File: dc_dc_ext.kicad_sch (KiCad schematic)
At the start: 30 parts, among them U10 TPS56339DDC, U11 TPS56339DDC

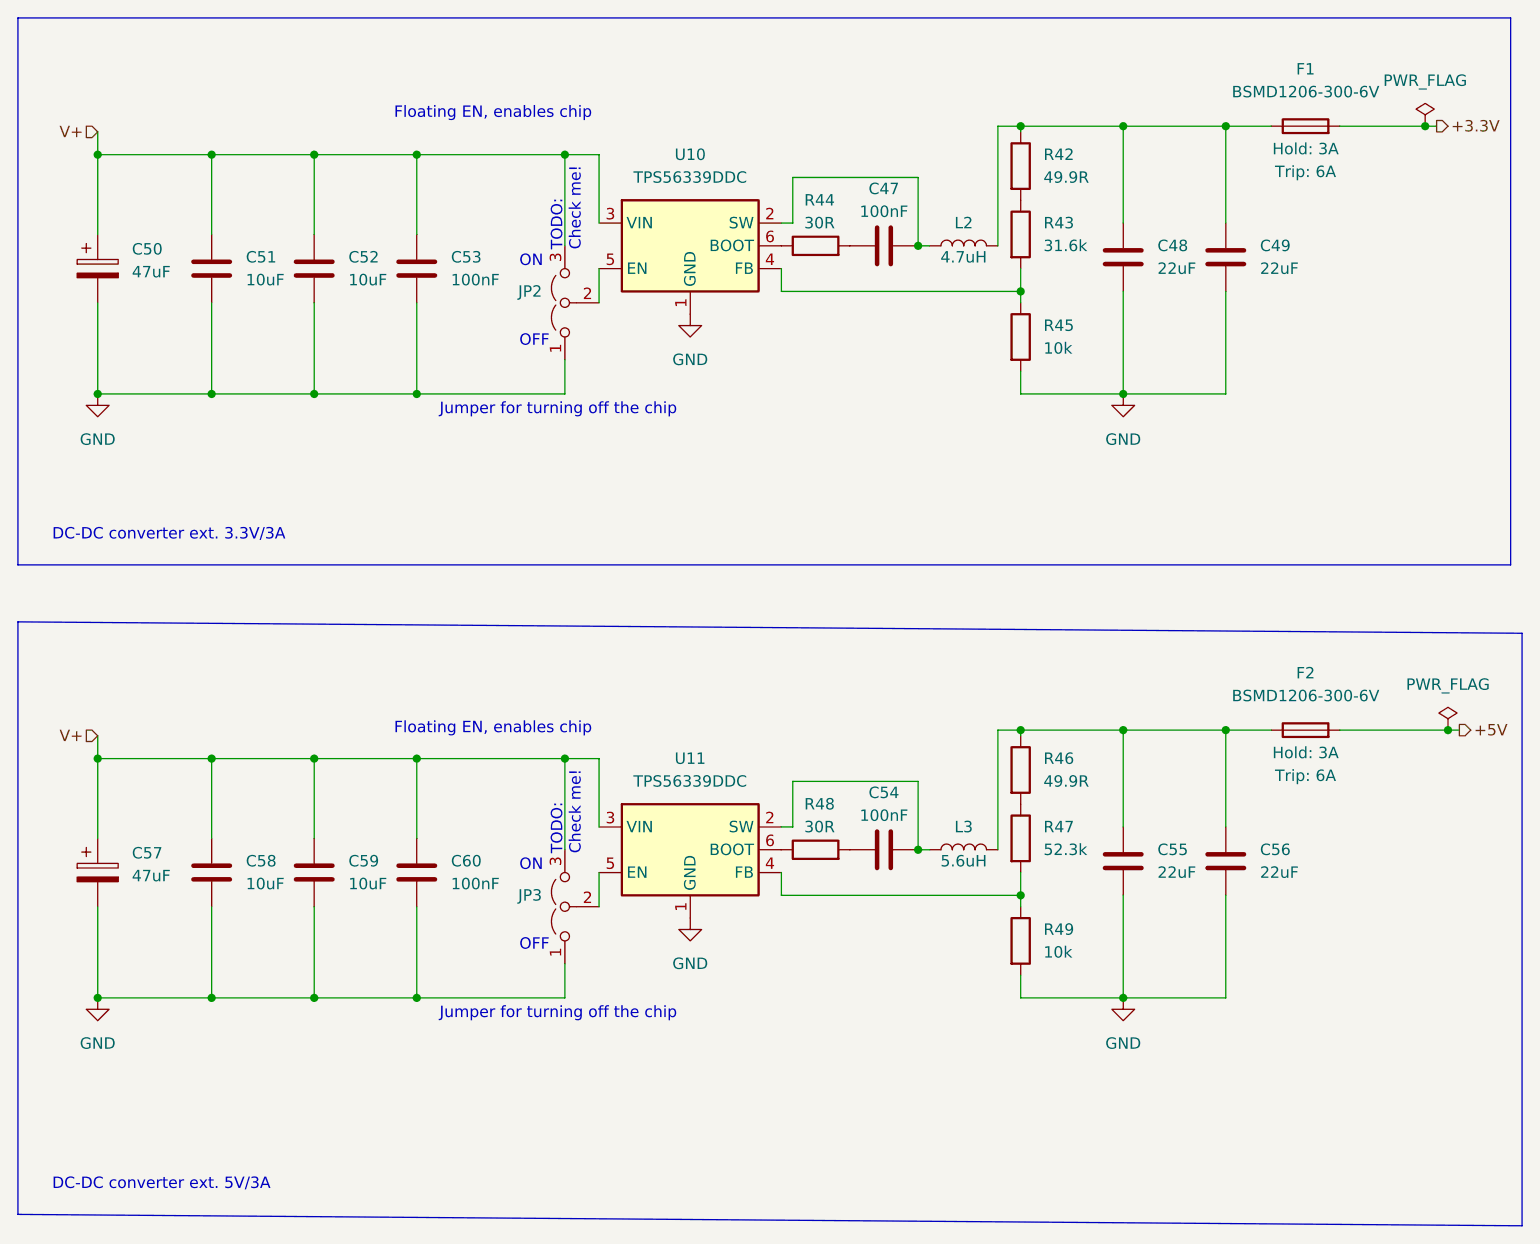
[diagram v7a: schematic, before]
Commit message: optimized component selection, assigned missing LCSC part numbers
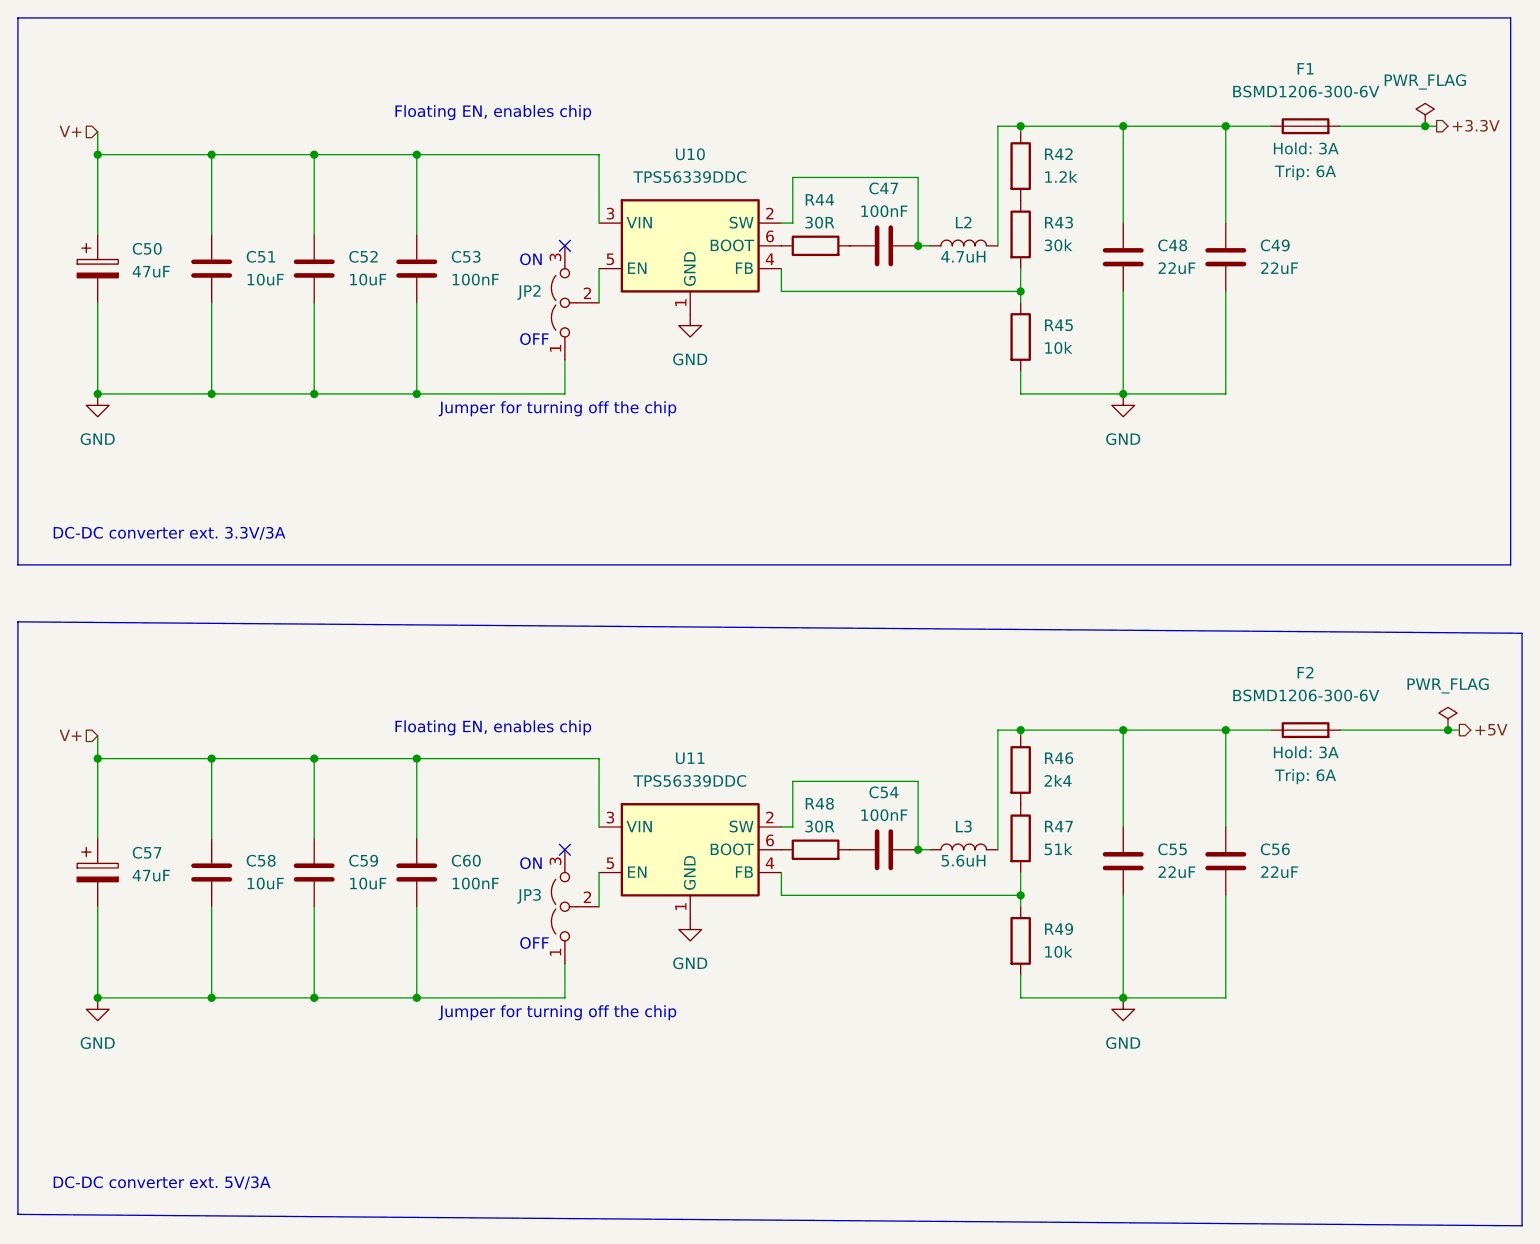
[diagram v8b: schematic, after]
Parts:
- C47, C53, C54, C60: footprint Capacitor_SMD:C_0805_2012Metric_Pad1.18x1.45mm_HandSolder -> Capacitor_SMD:C_0805_2012Metric
- C48, C49, C55, C56: footprint Capacitor_SMD:C_0805_2012Metric_Pad1.18x1.45mm_HandSolder -> Capacitor_SMD:C_1206_3216Metric; LCSC (none) -> C49217
- C50, C57: footprint Capacitor_SMD:CP_Elec_6.3x5.8 -> Capacitor_SMD:C_1206_3216Metric; LCSC (none) -> C403725
- C51, C52, C58, C59: footprint Capacitor_SMD:C_1206_3216Metric_Pad1.33x1.80mm_HandSolder -> Capacitor_SMD:C_1206_3216Metric; LCSC (none) -> C13585
- F1, F2: LCSC (none) -> C883136
- L2: LCSC (none) -> C167220
- L3: LCSC (none) -> C386869
- R42: value 49.9R -> 1.2k; footprint Resistor_SMD:R_0805_2012Metric_Pad1.20x1.40mm_HandSolder -> Resistor_SMD:R_0603_1608Metric; LCSC (none) -> C22765
- R43: value 31.6k -> 30k; footprint Resistor_SMD:R_0805_2012Metric_Pad1.20x1.40mm_HandSolder -> Resistor_SMD:R_0603_1608Metric; LCSC (none) -> C22984
- R44, R48: footprint Resistor_SMD:R_0805_2012Metric_Pad1.20x1.40mm_HandSolder -> Resistor_SMD:R_0603_1608Metric; LCSC (none) -> C23140
- R45, R49: footprint Resistor_SMD:R_0805_2012Metric_Pad1.20x1.40mm_HandSolder -> Resistor_SMD:R_0603_1608Metric; LCSC (none) -> C25804
- R46: value 49.9R -> 2k4; footprint Resistor_SMD:R_0805_2012Metric_Pad1.20x1.40mm_HandSolder -> Resistor_SMD:R_0603_1608Metric; LCSC (none) -> C22940
- R47: value 52.3k -> 51k; footprint Resistor_SMD:R_0805_2012Metric_Pad1.20x1.40mm_HandSolder -> Resistor_SMD:R_0603_1608Metric; LCSC (none) -> C23196
- U10, U11: LCSC (none) -> C2071106
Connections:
- net V+: no longer JP2.3 (B), JP3.3 (B)
- no-connect marks 0 -> 2
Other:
- note removed: "TODO: Check me!"
